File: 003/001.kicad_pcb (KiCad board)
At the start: 2 copper layers, 75 x 98.8 mm, 26 parts

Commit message: Add Firma to MKR Badge
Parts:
- removed the svg2mod at (143.0, 92.9)
- removed the svg2mod at (140.3, 98.4)
- added svg2mod: G***, ArduinoBadge:Firma.2019.CuMask.01, B.Cu at (163.2, 140.3)
- added svg2mod: G***, ArduinoBadge:2019.All.Mask.03, F.Cu at (140.3, 98.4)
- added svg2mod: G***, ArduinoBadge:2019.All.Mask.02, B.Cu at (143.0, 92.9)
- moved REF** 0.56 mm to (111.1, 78.8), turned to 90 degrees
- moved REF** 0.31 mm to (118.2, 129.9), turned to 90 degrees
- moved REF** 0.30 mm to (147.3, 99.4)
- moved REF** 0.30 mm to (138.4, 99.4)
- moved REF** 0.20 mm to (129.3, 77.4), turned to 90 degrees
- moved REF** 0.18 mm to (142.8, 131.3), turned to 90 degrees
- moved REF** 0.18 mm to (170.7, 119.5), turned to 90 degrees
- moved REF** 0.18 mm to (124.0, 55.9)
- moved REF** 0.05 mm to (147.3, 77.5), turned to 90 degrees

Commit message: Updates Mask
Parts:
- removed the svg2mod at (140.4, 55.0)
- removed the svg2mod at (140.1, 55.0)
- removed the svg2mod at (138.4, 77.5) (x4)
- removed the svg2mod at (140.3, 98.4) (x3)
- removed the svg2mod at (130.2, 77.5) (x2)
- removed the svg2mod at (146.7, 77.5) (x2)
- removed the svg2mod at (143.0, 92.9)
- added 2019.All.Mask.02: G***, ArduinoBadge:2019.All.Mask.02, B.Cu at (143.0, 92.9)
- added 2019.All.Mask.03: G***, ArduinoBadge:2019.All.Mask.03, F.Cu at (140.3, 98.4)
- added Arduino.SilkS: G***, ArduinoBadge:Arduino.SilkS, F.Cu at (138.4, 77.5)
- added Edge.Back.Only.SilkS.02: G***, ArduinoBadge:Edge.Back.Only.SilkS.02, B.Cu at (48.7, 127.9)
- added Edge.Only.SilkS.02: G***, ArduinoBadge:Edge.Only.SilkS.02, F.Cu at (46.4, 23.6)
- added Fig.04.Cu.Mask: G***, ArduinoBadge:Fig.04.Cu.Mask, F.Cu at (203.2, 107.3)
- added Fig.05.Cu.Mask: G***, ArduinoBadge:Fig.05.Cu.Mask, F.Cu at (201.3, 81.3)
- added Fig.06.Cu.Mask: G***, ArduinoBadge:Fig.06.Cu.Mask, F.Cu at (203.8, 126.4)
- added Holder.B.Cu.Mask.01: G***, ArduinoBadge:Holder.B.Cu.Mask.01, B.Cu at (140.0, 55.4)
- added Holder.Cu.Mask.01: G***, ArduinoBadge:Holder.Cu.Mask.01, F.Cu at (140.0, 55.0)
- added logo.B.Mask.Der.01: logo.B.Mask.Der.01, ArduinoBadge:logo.B.Mask.Der.01, B.Cu at (203.2, 41.9)
- added logo.B.Mask.Izq.01: logo.B.Mask.Izq.01, ArduinoBadge:logo.B.Mask.Izq.01, B.Cu at (181.6, 41.9)
- added logo.F.Mask.Der.01: G***, ArduinoBadge:logo.F.Mask.Der.01, F.Cu at (196.8, 62.2)
- added logo.F.Mask.Izq.01: G***, ArduinoBadge:logo.F.Mask.Izq.01, F.Cu at (181.0, 62.2)

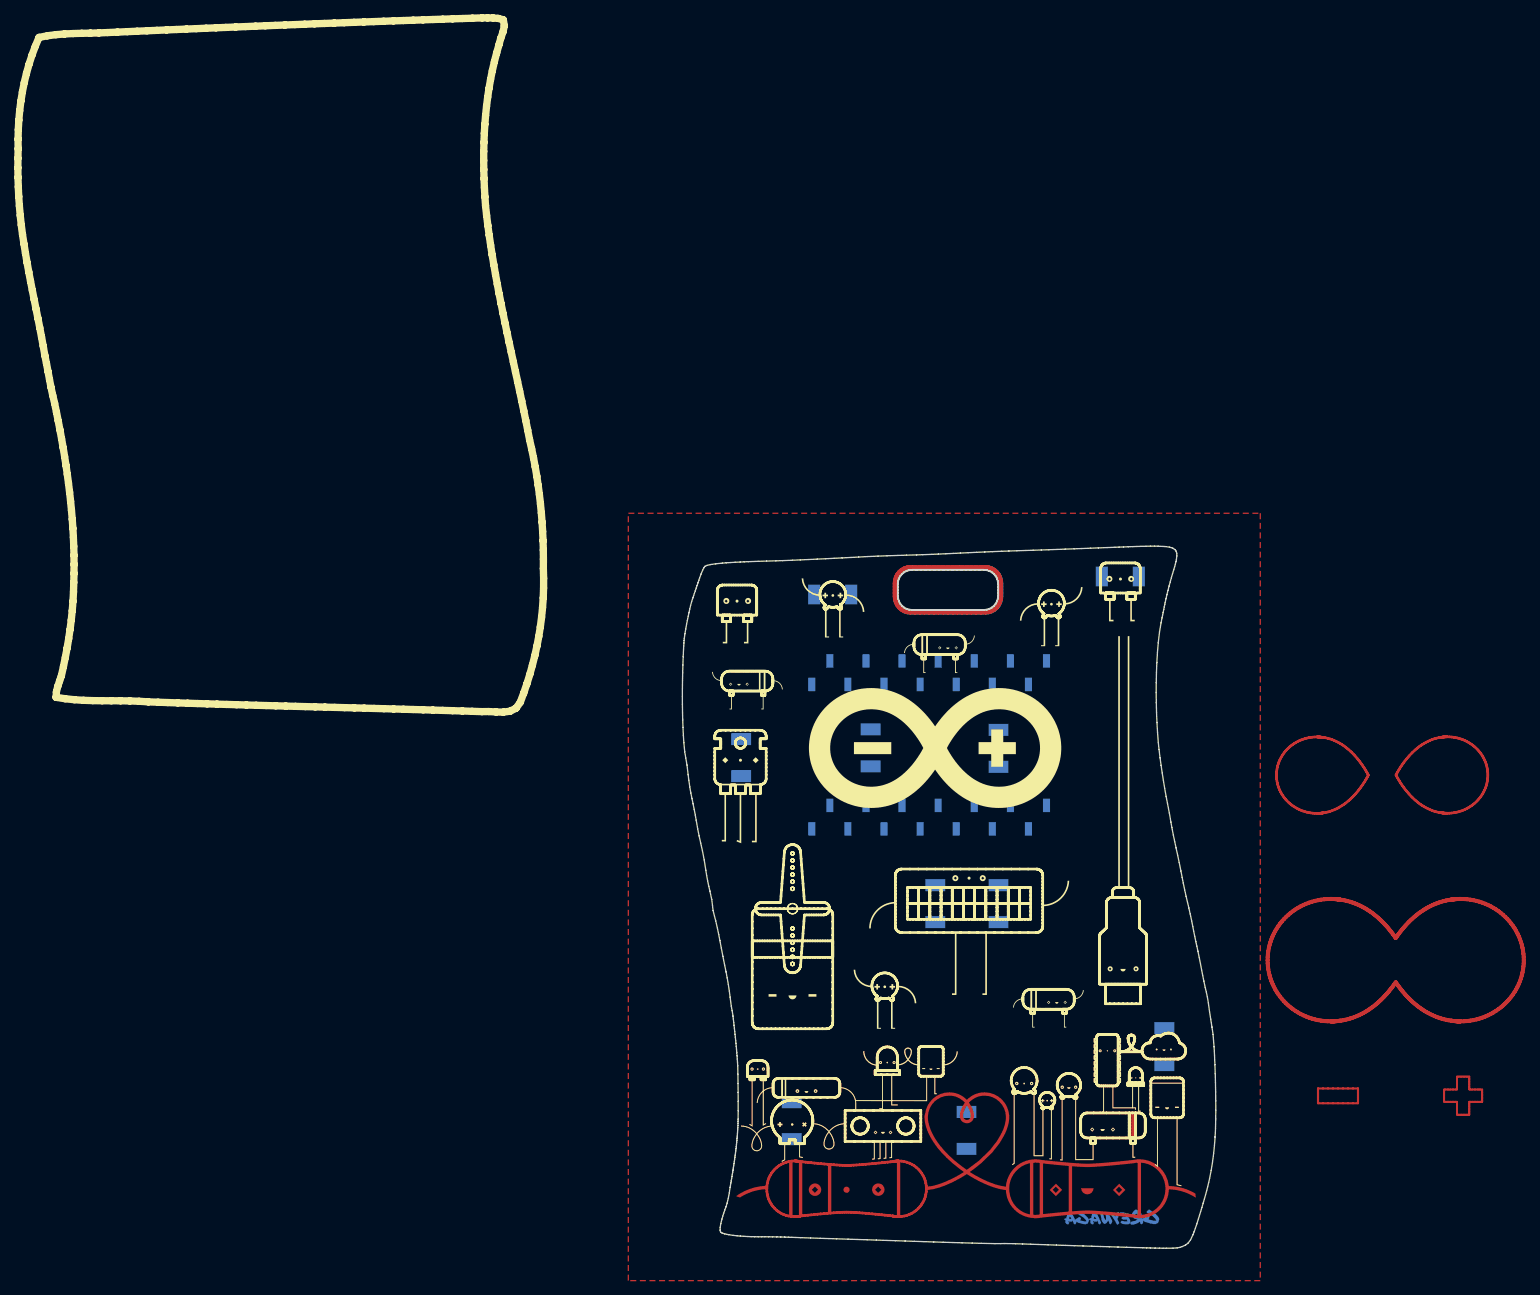
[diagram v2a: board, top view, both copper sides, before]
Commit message: Add Footprint MKR Family
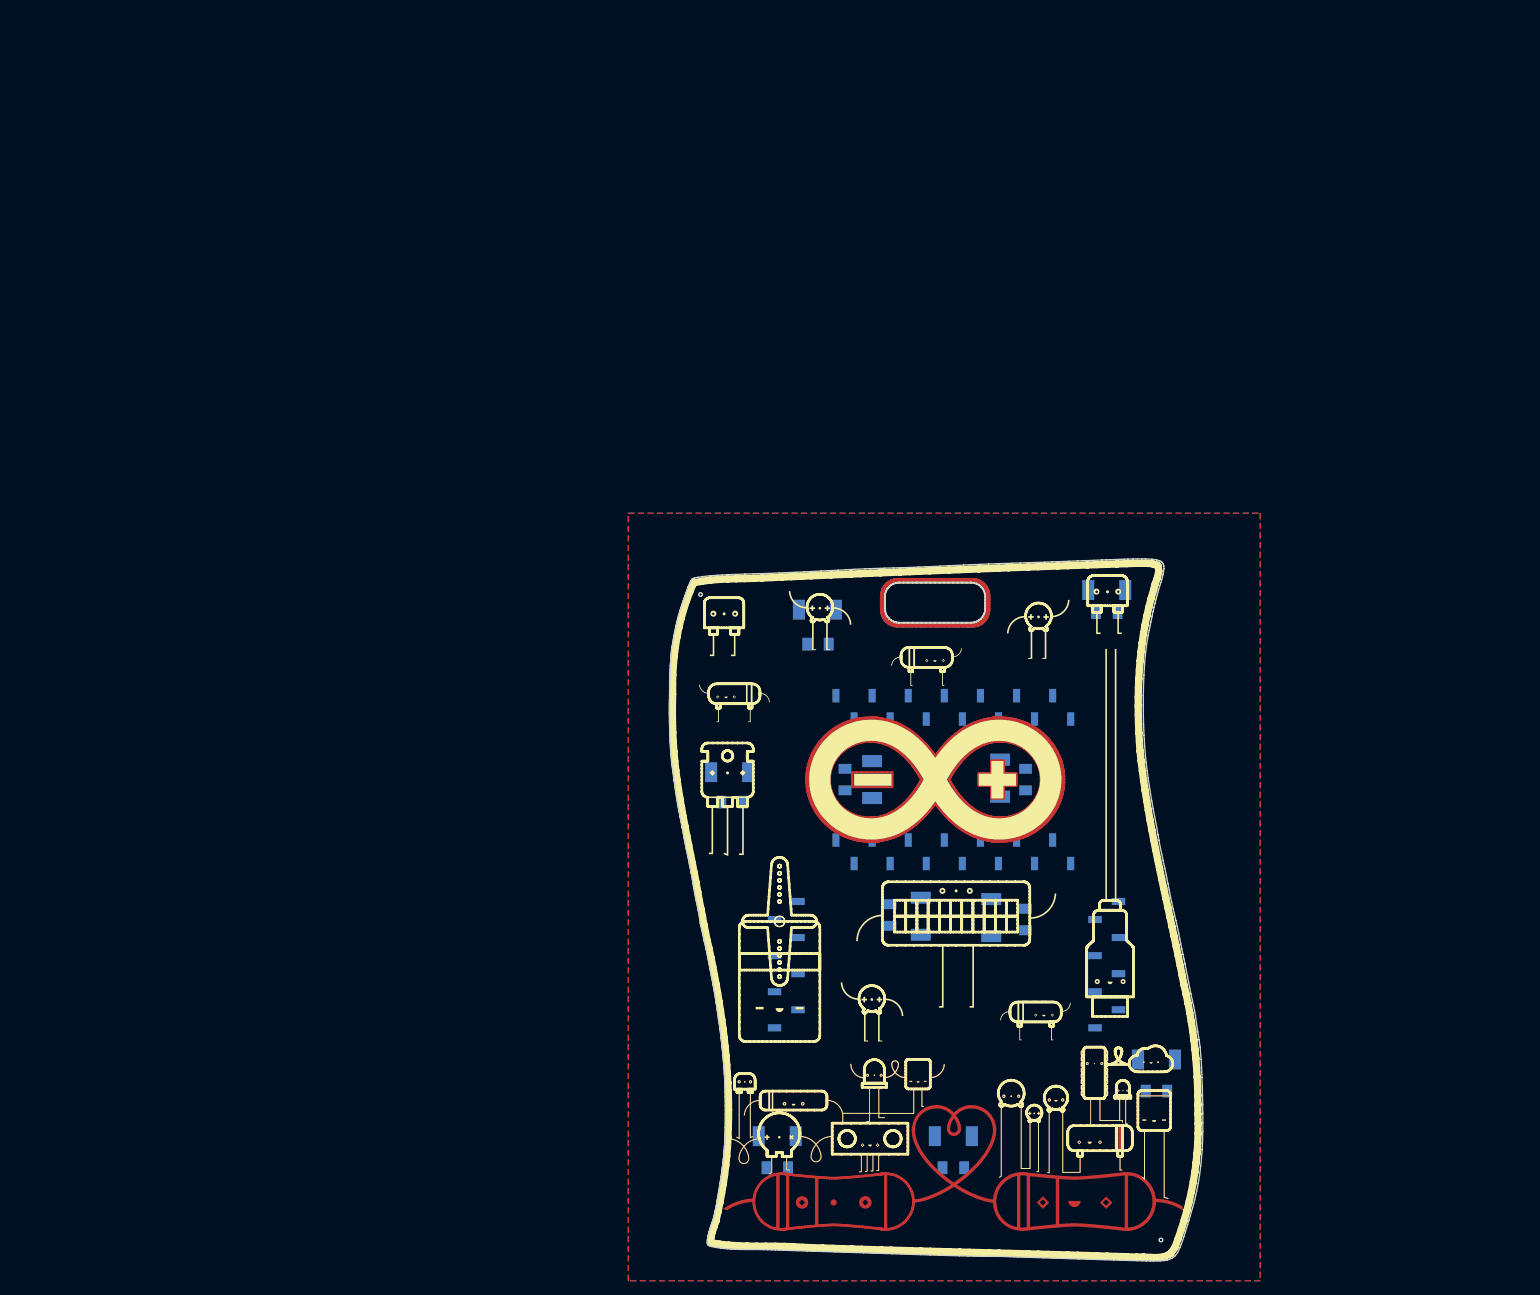
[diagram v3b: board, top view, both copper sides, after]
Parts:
- removed 2019.All.Mask.02: G***, ArduinoBadge:2019.All.Mask.02
- removed 2019.All.Mask.03: G***, ArduinoBadge:2019.All.Mask.03
- removed Arduino.SilkS: G***, ArduinoBadge:Arduino.SilkS
- removed Edge.Back.Only.SilkS.02: G***, ArduinoBadge:Edge.Back.Only.SilkS.02
- removed Edge.Only.SilkS.02: G***, ArduinoBadge:Edge.Only.SilkS.02
- removed Fig.04.Cu.Mask: G***, ArduinoBadge:Fig.04.Cu.Mask
- removed Fig.05.Cu.Mask: G***, ArduinoBadge:Fig.05.Cu.Mask
- removed Fig.06.Cu.Mask: G***, ArduinoBadge:Fig.06.Cu.Mask
- removed Holder.B.Cu.Mask.01: G***, ArduinoBadge:Holder.B.Cu.Mask.01
- removed Holder.Cu.Mask.01: G***, ArduinoBadge:Holder.Cu.Mask.01
- removed REF** (x10): SunLed_Reverse-2, ArduinoBadge:SunLed_PLCC_Reverse-2
- removed REF** (x2): PinSocket_1x14_P2.54mm_Vertical_SMD_Pin1Right, Connector_PinSocket_2.54mm:PinSocket_1x14_P2.54mm_Vertical_SMD_Pin1Right
- removed logo.B.Mask.Der.01: logo.B.Mask.Der.01, ArduinoBadge:logo.B.Mask.Der.01
- removed logo.B.Mask.Izq.01: logo.B.Mask.Izq.01, ArduinoBadge:logo.B.Mask.Izq.01
- removed logo.F.Mask.Der.01: G***, ArduinoBadge:logo.F.Mask.Der.01
- removed logo.F.Mask.Izq.01: G***, ArduinoBadge:logo.F.Mask.Izq.01
- removed svg2mod: G***, ArduinoBadge:Firma.2019.CuMask.01
- added D1: LED_ALT, ArduinoBadge:SunLed_PLCC_Reverse-2, B.Cu at (136.4, 101.1)
- added D10: LED_ALT, ArduinoBadge:SunLed_PLCC_Reverse-2, B.Cu at (116.2, 132.1)
- added D2: LED_ALT, ArduinoBadge:SunLed_PLCC_Reverse-2, B.Cu at (109.5, 80.9)
- added D3: LED_ALT, ArduinoBadge:SunLed_PLCC_Reverse-2, B.Cu at (121.8, 58.0)
- added D4: LED_ALT, ArduinoBadge:SunLed_PLCC_Reverse-2, B.Cu at (147.5, 81.7)
- added D5: LED_ALT, ArduinoBadge:SunLed_PLCC_Reverse-2, B.Cu at (129.5, 81.9)
- added D6: LED_ALT, ArduinoBadge:SunLed_PLCC_Reverse-2, B.Cu at (162.6, 55.2)
- added D7: LED_ALT, ArduinoBadge:SunLed_PLCC_Reverse-2, B.Cu at (169.5, 121.3)
- added D8: LED_ALT, ArduinoBadge:SunLed_PLCC_Reverse-2, B.Cu at (141.0, 132.1)
- added D9: LED_ALT, ArduinoBadge:SunLed_PLCC_Reverse-2, B.Cu at (146.3, 101.3)
- added J1: CONN_01X08, Connector_PinSocket_2.54mm:PinSocket_1x08_P2.54mm_Vertical_SMD_Pin1Left, B.Cu at (117.5, 108.0)
- added J2: CONN_01X08, Connector_PinSocket_2.54mm:PinSocket_1x08_P2.54mm_Vertical_SMD_Pin1Left, B.Cu at (162.6, 108.0)
- added R1: R, Resistor_SMD:R_1206_3216Metric_Pad1.39x1.80mm_HandSolder, B.Cu at (132.1, 101.0)
- added R10: R, Resistor_SMD:R_1206_3216Metric_Pad1.39x1.80mm_HandSolder, B.Cu at (116.2, 136.5)
- added R2: R, Resistor_SMD:R_1206_3216Metric_Pad1.39x1.80mm_HandSolder, B.Cu at (109.9, 85.1)
- added R3: R, Resistor_SMD:R_1206_3216Metric_Pad1.39x1.80mm_HandSolder, B.Cu at (121.9, 62.9)
- added R4: R, Resistor_SMD:R_1206_3216Metric_Pad1.39x1.80mm_HandSolder, B.Cu at (151.1, 81.9)
- added R5: R, Resistor_SMD:R_1206_3216Metric_Pad1.39x1.80mm_HandSolder, B.Cu at (125.7, 81.9)
- added R6: R, Resistor_SMD:R_1206_3216Metric_Pad1.39x1.80mm_HandSolder, B.Cu at (162.6, 58.4)
- added R7: R, Resistor_SMD:R_1206_3216Metric_Pad1.39x1.80mm_HandSolder, B.Cu at (169.5, 125.7)
- added R8: R, Resistor_SMD:R_1206_3216Metric_Pad1.39x1.80mm_HandSolder, B.Cu at (141.0, 136.5)
- added R9: R, Resistor_SMD:R_1206_3216Metric_Pad1.39x1.80mm_HandSolder, B.Cu at (151.1, 101.6)
- added U1: 2019.All.Mask.02, ArduinoBadge:2019.All.Mask.02, B.Cu at (141.1, 94.7)
- added U10: Holder.Cu.Mask.01, ArduinoBadge:Holder.Cu.Mask.01, F.Cu at (138.2, 56.8)
- added U11: logo.B.Mask.Der.01, ArduinoBadge:logo.B.Mask.Der.01, B.Cu at (146.9, 81.9)
- added U12: logo.B.Mask.Izq.01, ArduinoBadge:logo.B.Mask.Izq.01, B.Cu at (130.1, 81.9)
- added U13: logo.F.Mask.Der.01, ArduinoBadge:logo.F.Mask.Der.01, F.Cu at (146.6, 81.9)
- added U14: logo.F.Mask.Izq.01, ArduinoBadge:logo.F.Mask.Izq.01, F.Cu at (130.1, 82.0)
- added U15: MKR_Family, ArduinoBadge:MKR_Family_SMD, B.Cu at (141.0, 81.9)
- added U2: 2019.All.Mask.03, ArduinoBadge:2019.All.Mask.03, F.Cu at (138.5, 100.2)
- added U3: Arduino.SilkS, ArduinoBadge:Arduino.SilkS, F.Cu at (138.4, 81.9)
- added U4: Edge.Back.Only.SilkS.02, ArduinoBadge:Edge.Back.Only.SilkS.02, B.Cu at (138.4, 100.3)
- added U5: Edge.Only.SilkS.02, ArduinoBadge:Edge.Only.SilkS.02, F.Cu at (138.4, 100.3)
- added U6: Fig.04.Cu.Mask, ArduinoBadge:Fig.04.Cu.Mask, F.Cu at (138.4, 81.9)
- added U7: Fig.05.Cu.Mask, ArduinoBadge:Fig.05.Cu.Mask, F.Cu at (138.4, 81.9)
- added U8: Fig.06.Cu.Mask, ArduinoBadge:Fig.06.Cu.Mask, F.Cu at (138.3, 81.9)
- added U9: Holder.B.Cu.Mask.01, ArduinoBadge:Holder.B.Cu.Mask.01, B.Cu at (138.6, 56.8)
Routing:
- net GND: vias 0 -> 2
- added copper zone on B.Cu, net GND
- added copper zone on F.Cu, net GND
- removed copper zone on F.Cu, net (none)
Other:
- outline, holes or cut-outs redrawn

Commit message: Updates
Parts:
- moved J1 42.1 mm to (141.0, 73.0), turned to 270 degrees
- moved J2 25.4 mm to (141.0, 121.3), turned to 270 degrees
- moved U15 19.0 mm to (141.0, 101.0)
- moved R8 8.35 mm to (132.7, 135.3), turned to 180 degrees
- moved R4 3.81 mm to (154.9, 81.9)
- moved R5 3.81 mm to (121.9, 81.9)
- moved R6 1.27 mm to (162.6, 59.7)
- moved R2 0.90 mm to (109.2, 85.7)
- moved R1 0.64 mm to (131.4, 101.0)
- moved R9 0.63 mm to (151.1, 101.0)
- moved D2 0.28 mm to (109.2, 80.9)
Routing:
- net /~D5: track 0.00 -> 40.9 mm
- net Net-(D5-Pad1): track 0.00 -> 13.3 mm
- net Net-(D4-Pad1): track 0.00 -> 12.6 mm
- net Net-(D9-Pad1): track 0.00 -> 9.84 mm
- net Net-(D7-Pad1): track 0.00 -> 9.74 mm
- net Net-(D10-Pad1): track 0.00 -> 9.74 mm
- net Net-(D2-Pad1): track 0.00 -> 9.65 mm
- net Net-(D6-Pad1): track 0.00 -> 9.61 mm
- net Net-(D1-Pad1): track 0.00 -> 9.28 mm
- net Net-(D8-Pad1): track 0.00 -> 6.71 mm
- net Net-(D3-Pad1): track 0.00 -> 5.34 mm
- net GND: vias 2 -> 1
- removed copper zone on F.Cu, net GND
